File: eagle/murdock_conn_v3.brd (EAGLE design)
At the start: 47 x 31.8 mm, 12 parts, among them X1 GPS, X2 IMU, X7 MURDOCK_STACK

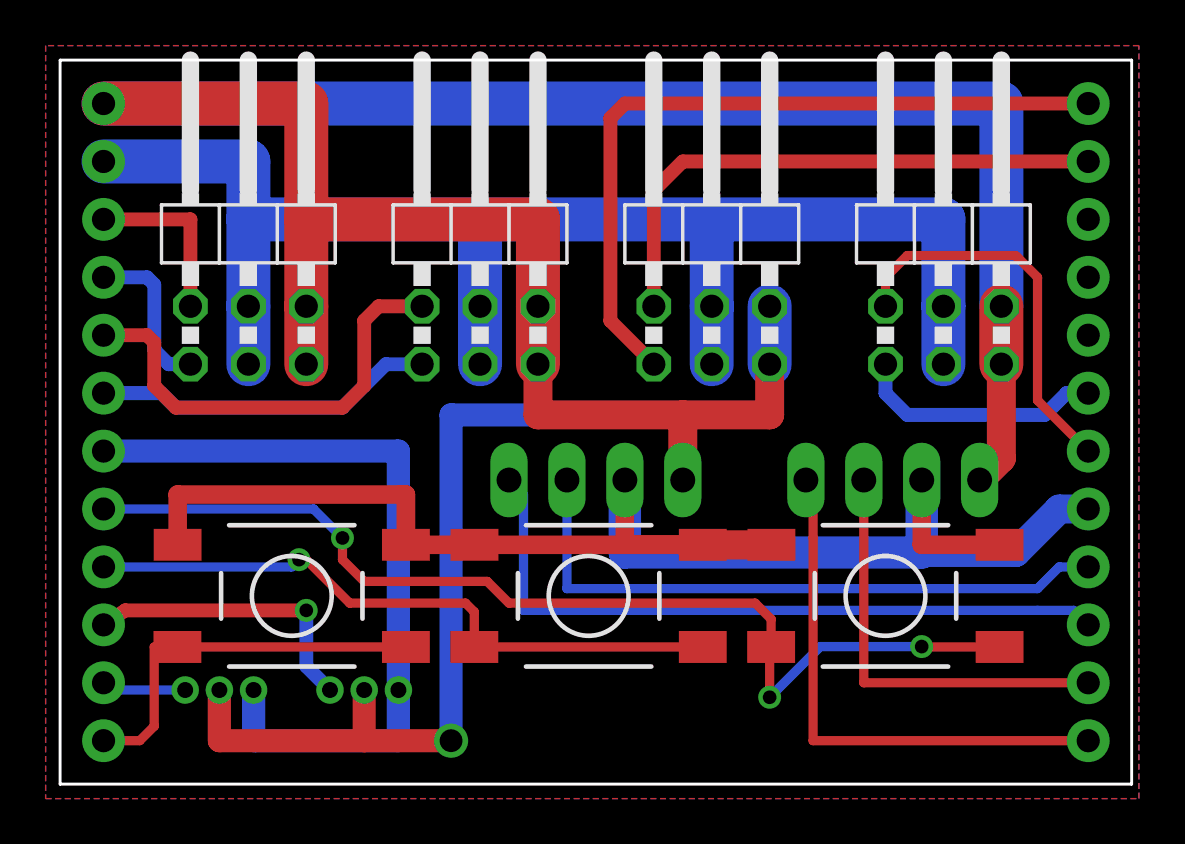
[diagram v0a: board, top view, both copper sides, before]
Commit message: moved servo connectors
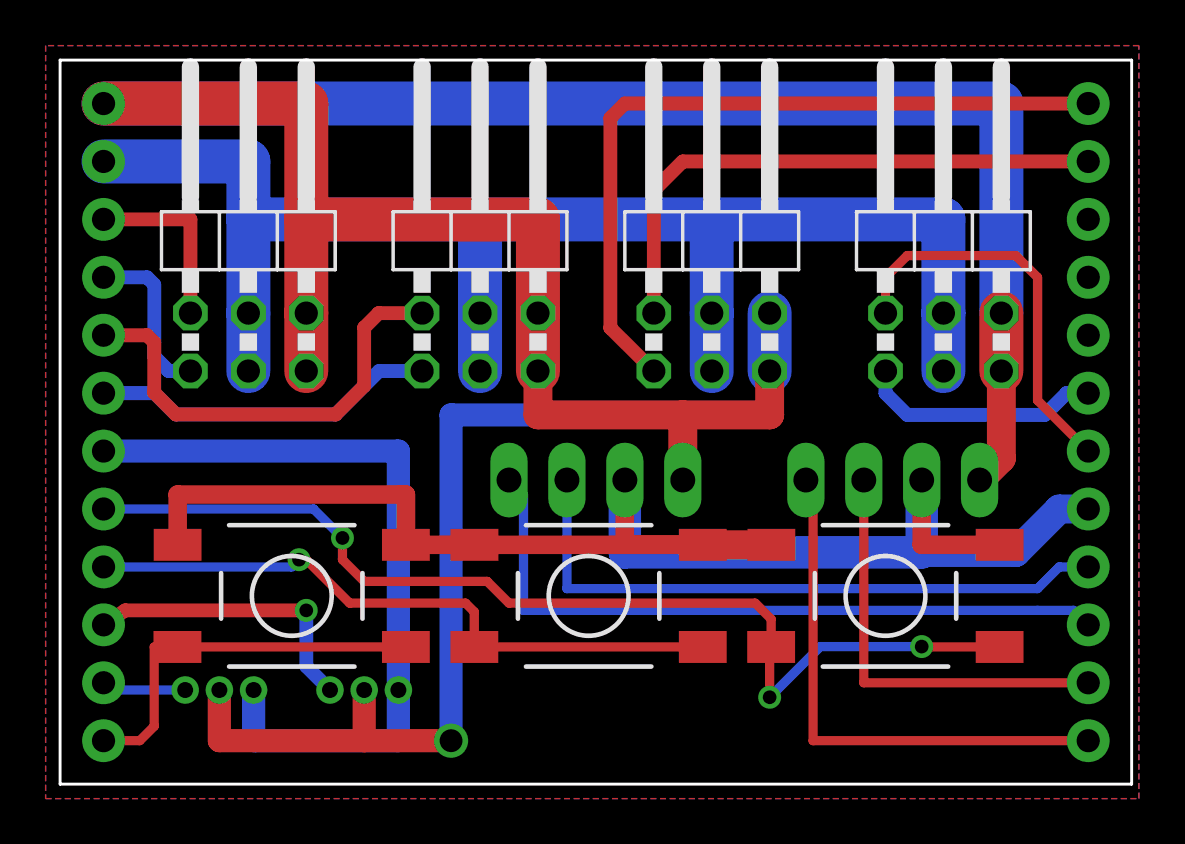
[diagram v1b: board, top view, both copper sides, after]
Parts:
- moved X3 0.30 mm to (28.6, 24.5)
- moved X4 0.30 mm to (18.4, 24.5)
- moved X5 0.30 mm to (8.26, 24.5)
- moved X6 0.30 mm to (38.7, 24.5)
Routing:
- net 5V: track 64.8 -> 66.0 mm

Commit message: switch part-numbers
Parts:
- S1, S2, S3: value (none) -> min: "taster 9318" max: "taster 9319"
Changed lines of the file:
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@@
 <element name="U$10" library="seb" package="S3B-ZR" value="S3B-ZR" x="6.985" y="4.1275" smashed="yes" rot="MR0"/>
 <element name="U$11" library="seb" package="S3B-ZR" value="S3B-ZR" x="13.335" y="4.1275" smashed="yes" rot="MR0"/>
-<element name="S2" library="switch-tact" package="LSH" value="" x="36.195" y="8.255" smashed="yes" rot="R180">
+<element name="S2" library="switch-tact" package="LSH" value="min: &quot;taster 9318&quot; max: &quot;taster 9319&quot;" x="36.195" y="8.255" smashed="yes" rot="R180">
 <attribute name="VALUE" x="38.735" y="13.335" size="1.27" layer="27" rot="R180"/>
 </element>
-<element name="S1" library="switch-tact" package="LSH" value="" x="10.16" y="8.255" smashed="yes" rot="R180">
+<element name="S1" library="switch-tact" package="LSH" value="min: &quot;taster 9318&quot; max: &quot;taster 9319&quot;" x="10.16" y="8.255" smashed="yes" rot="R180">
 <attribute name="VALUE" x="12.7" y="13.335" size="1.27" layer="27" rot="R180"/>
 </element>
-<element name="S3" library="switch-tact" package="LSH" value="" x="23.1775" y="8.255" smashed="yes" rot="R180">
+<element name="S3" library="switch-tact" package="LSH" value="min: &quot;taster 9318&quot; max: &quot;taster 9319&quot;" x="23.1775" y="8.255" smashed="yes" rot="R180">
 <attribute name="VALUE" x="25.7175" y="13.335" size="1.27" layer="27" rot="R180"/>
 </element>
